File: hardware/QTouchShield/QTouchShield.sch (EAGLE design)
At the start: 114 parts, among them IC1 AT32UC3C0512CJEDEC-MS-026, U1 ARDUINO-MEGALITE

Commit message: Added cuttable bridges for RESET and SPI.
Added cuttable PCB bridges that allow default:
- RESET switch of shield connected to RESET of Arduino
- SPI interface selected as default interface
Defaults can be changed by cutting the bridges through with a scalpel.
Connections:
- removed net MISO-PIN50: SJ4.1, U1.50
- removed net MOSI-PIN51: SJ3.1, U1.51
- removed net N$34: SJ5.1, U1.RESET
- removed net SCK-PIN52: SJ2.1, U1.52
- removed net SS-PIN53: SJ1.1, U1.53
- net JTAG_RESET: now also SJ5.1, U1.RESET
- net SDT-SPI0-MISO: now also SJ3.1, U1.51
- net SDT-SPI0-MOSI: now also SJ4.1, U1.50
- net SDT-SPI0-SCK: now also SJ2.1, U1.52
- net SDT-SPI0-SS: now also SJ1.1, U1.53
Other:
- note added: "Cut wires to use"
- note added: "Date: 12th July 2012"
- note added: "Revision: 0.3"
- note removed: "Date: 8th June 2012"
- note removed: "Remove links to use"
- note removed: "Revision: 0.2"

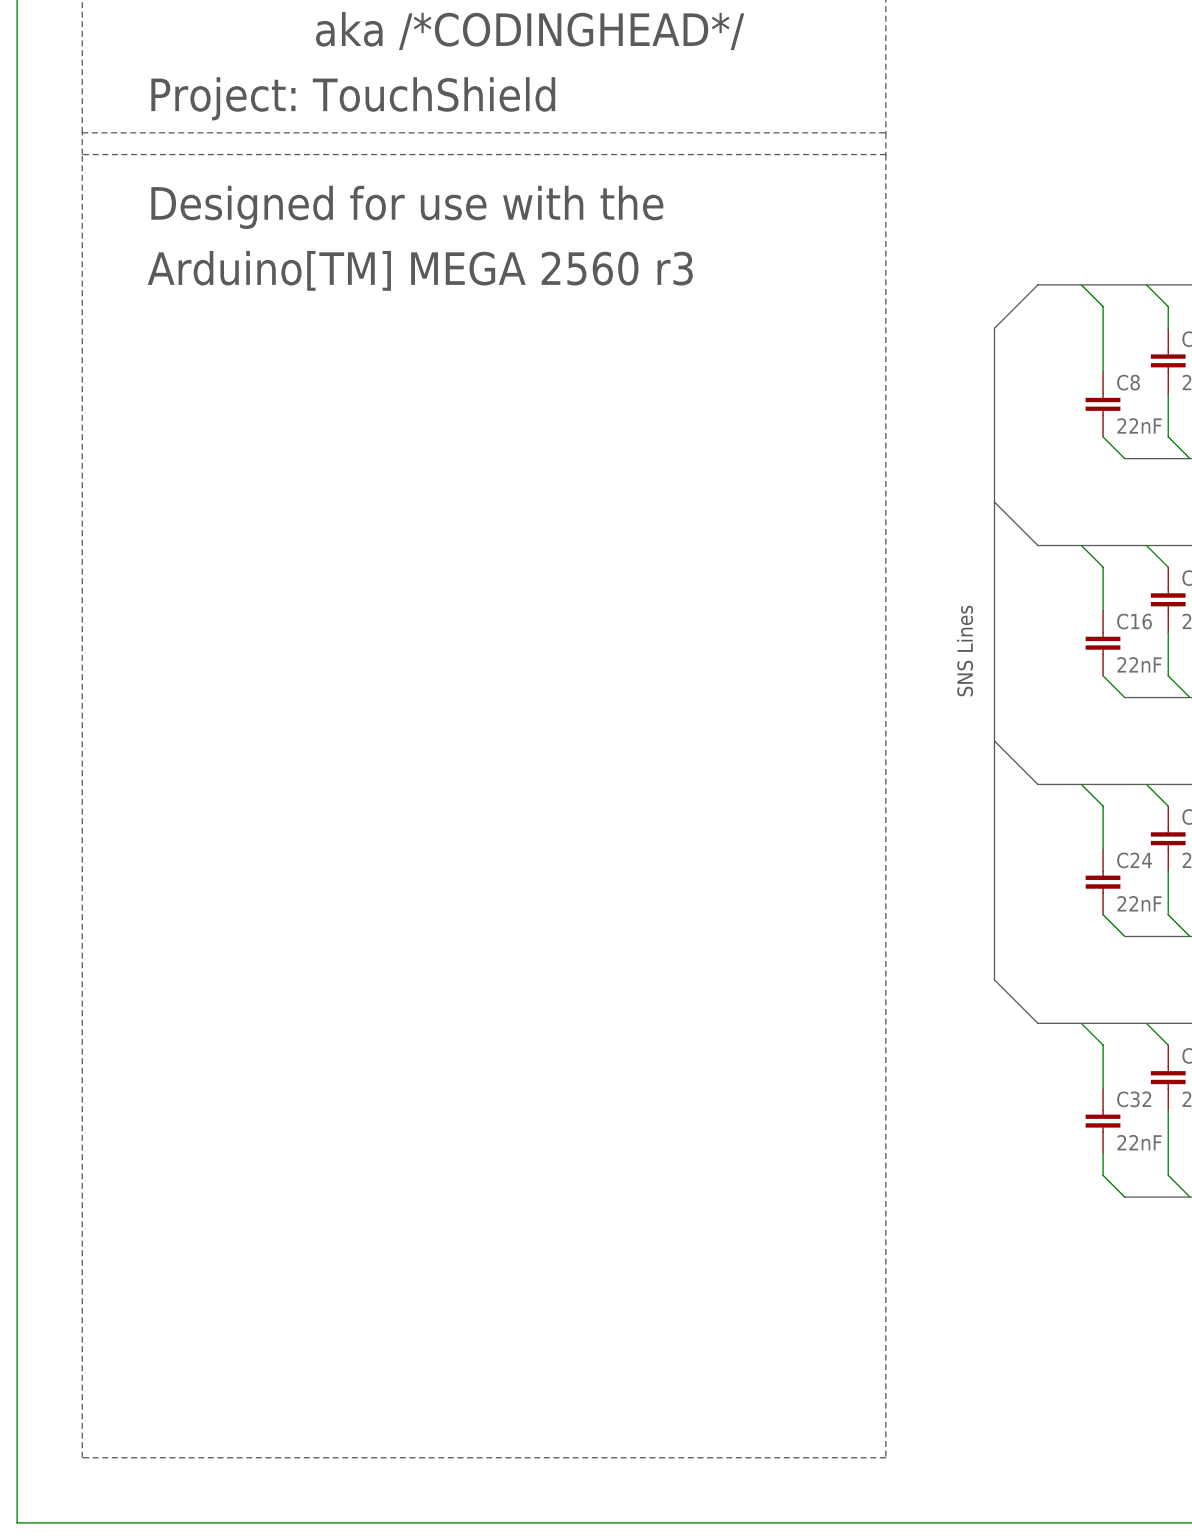
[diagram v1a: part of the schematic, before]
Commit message: Added license text to schematic.
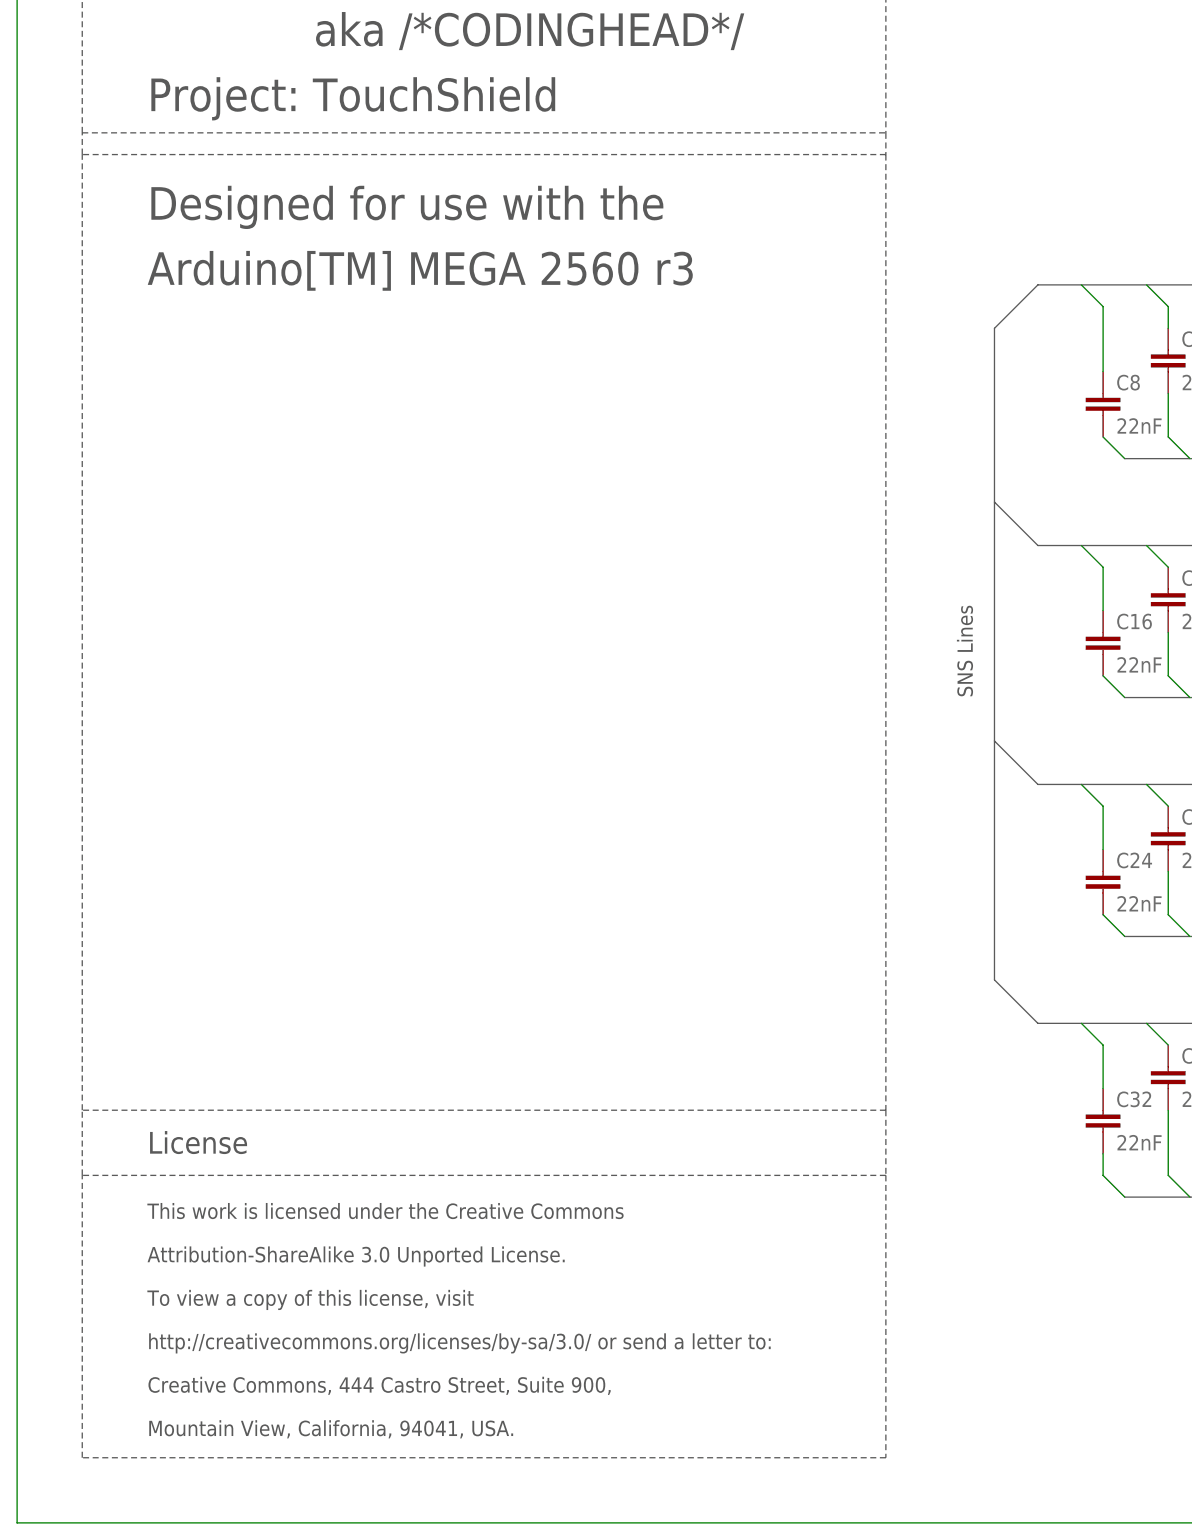
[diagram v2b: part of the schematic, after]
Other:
- note added: "Attribution-ShareAlike 3.0 Unported License."
- note added: "Creative Commons, 444 Castro Street, Suite 900,"
- note added: "License"
- note added: "Mountain View, California, 94041, USA."
- note added: "This work is licensed under the Creative Commons"
- note added: "To view a copy of this license, visit"
- note added: "http://creativecommons.org/licenses/by-sa/3.0/ or send a letter to:"
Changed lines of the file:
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@@
 <wire x1="-96.52" y1="-66.04" x2="-2.54" y2="-66.04" width="0.1524" layer="97" style="shortdash"/>
 <wire x1="-2.54" y1="-66.04" x2="-2.54" y2="-106.68" width="0.1524" layer="97" style="shortdash"/>
-<wire x1="-2.54" y1="-109.22" x2="-2.54" y2="-261.62" width="0.1524" layer="97" style="shortdash"/>
+<wire x1="-2.54" y1="-109.22" x2="-2.54" y2="-220.98" width="0.1524" layer="97" style="shortdash"/>
+<wire x1="-2.54" y1="-220.98" x2="-2.54" y2="-228.6" width="0.1524" layer="97" style="shortdash"/>
+<wire x1="-2.54" y1="-228.6" x2="-2.54" y2="-261.62" width="0.1524" layer="97" style="shortdash"/>
 <wire x1="-2.54" y1="-261.62" x2="-96.52" y2="-261.62" width="0.1524" layer="97" style="shortdash"/>
-<wire x1="-96.52" y1="-261.62" x2="-96.52" y2="-109.22" width="0.1524" layer="97" style="shortdash"/>
+<wire x1="-96.52" y1="-261.62" x2="-96.52" y2="-228.6" width="0.1524" layer="97" style="shortdash"/>
+<wire x1="-96.52" y1="-228.6" x2="-96.52" y2="-220.98" width="0.1524" layer="97" style="shortdash"/>
+<wire x1="-96.52" y1="-220.98" x2="-96.52" y2="-109.22" width="0.1524" layer="97" style="shortdash"/>
 <wire x1="-96.52" y1="-106.68" x2="-96.52" y2="-66.04" width="0.1524" layer="97" style="shortdash"/>
 <wire x1="-96.52" y1="-106.68" x2="-2.54" y2="-106.68" width="0.1524" layer="97" style="shortdash"/>
@@
 <rectangle x1="305.35" y1="-245.15" x2="365.35" y2="-245.05" layer="200"/>
 <rectangle x1="305.35" y1="-245.05" x2="365.35" y2="-244.95" layer="200"/>
+<text x="-88.9" y="-259.08" size="1.778" layer="97">Mountain View, California, 94041, USA.</text>
+<text x="-88.9" y="-254" size="1.778" layer="97">Creative Commons, 444 Castro Street, Suite 900,</text>
+<text x="-88.9" y="-248.92" size="1.778" layer="97">http://creativecommons.org/licenses/by-sa/3.0/ or send a letter to:</text>
+<text x="-88.9" y="-243.84" size="1.778" layer="97">To view a copy of this license, visit</text>
+<text x="-88.9" y="-238.76" size="1.778" layer="97">Attribution-ShareAlike 3.0 Unported License.</text>
+<text x="-88.9" y="-233.68" size="1.778" layer="97">This work is licensed under the Creative Commons</text>
+<text x="-88.9" y="-226.06" size="2.54" layer="97">License</text>
+<wire x1="-2.54" y1="-228.6" x2="-96.52" y2="-228.6" width="0.1524" layer="97" style="shortdash"/>
+<wire x1="-2.54" y1="-220.98" x2="-96.52" y2="-220.98" width="0.1524" layer="97" style="shortdash"/>
 </plain>
 <instances>
